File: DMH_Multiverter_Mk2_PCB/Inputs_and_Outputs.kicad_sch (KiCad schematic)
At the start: 27 parts, among them J1 TS_Jack_6.35mm_Sw, J10 TS_Jack_6.35mm_Sw, J11 TS_Jack_6.35mm_Sw, J12 TS_Jack_6.35mm_Sw, J13 TS_Jack_6.35mm_Sw, J14 TS_Jack_6.35mm_Sw, J15 TS_Jack_6.35mm_Sw, J16 TS_Jack_6.35mm_Sw, J17 TS_Jack_6.35mm_Sw, J18 TS_Jack_6.35mm_Sw, J19 TS_Jack_6.35mm_Sw, J2 TS_Jack_6.35mm_Sw, J20 TS_Jack_6.35mm_Sw, J200 BackBone_Connector_6pin, J21 TS_Jack_6.35mm_Sw, J22 TS_Jack_6.35mm_Sw, J3 TS_Jack_6.35mm_Sw, J4 TS_Jack_6.35mm_Sw, J5 TS_Jack_6.35mm_Sw, J50 Conn_01x06, J6 TS_Jack_6.35mm_Sw, J60 Conn_01x06, J7 TS_Jack_6.35mm_Sw, J8 TS_Jack_6.35mm_Sw, J9 TS_Jack_6.35mm_Sw

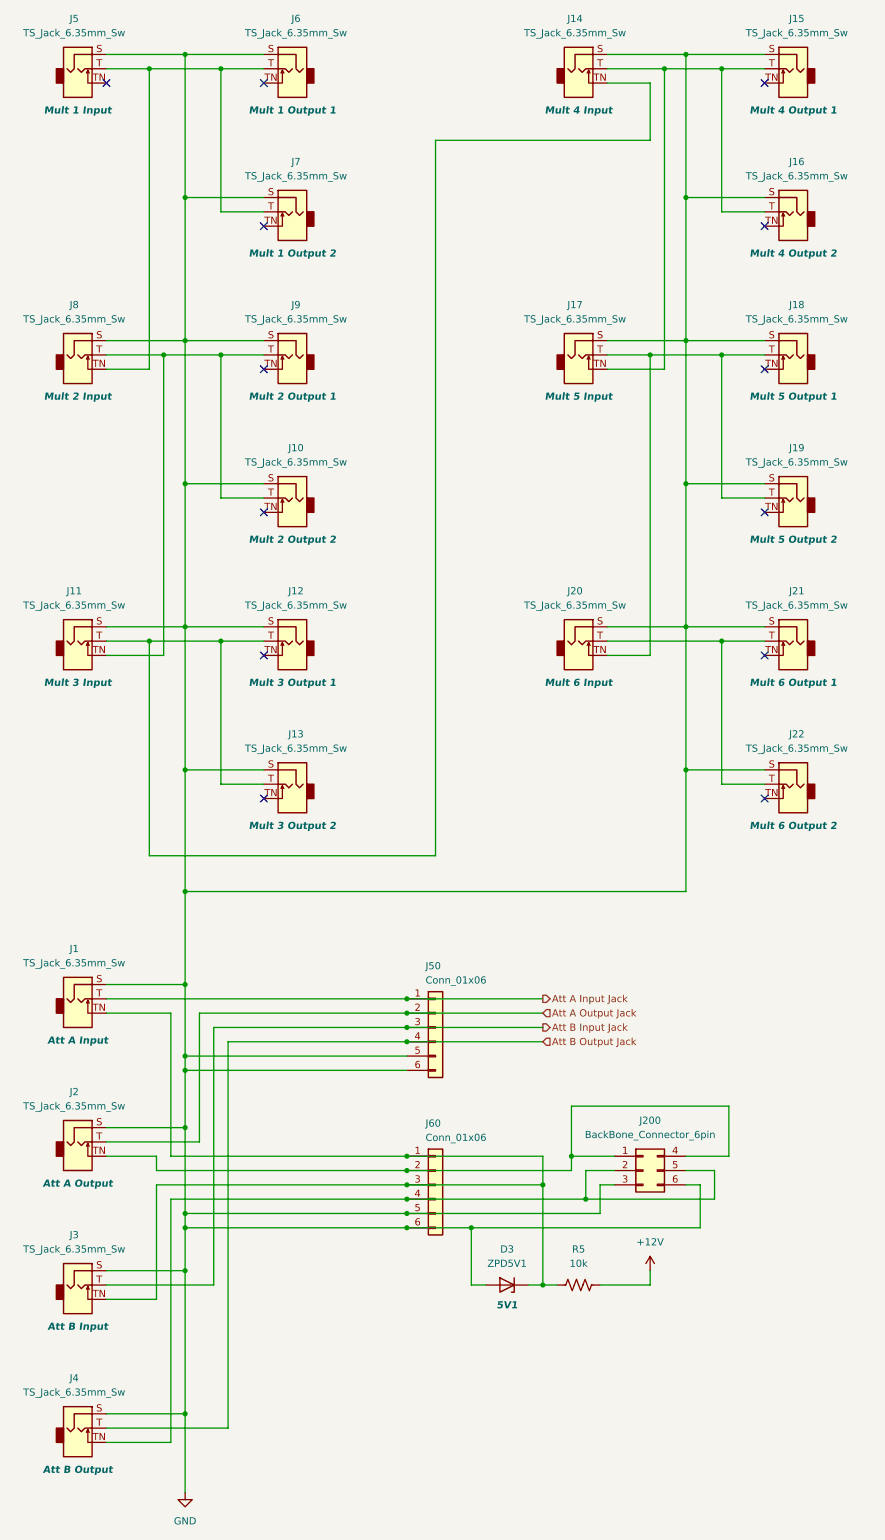
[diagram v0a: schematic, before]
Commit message: Added 3rd attenuverter to Panel and Schematic
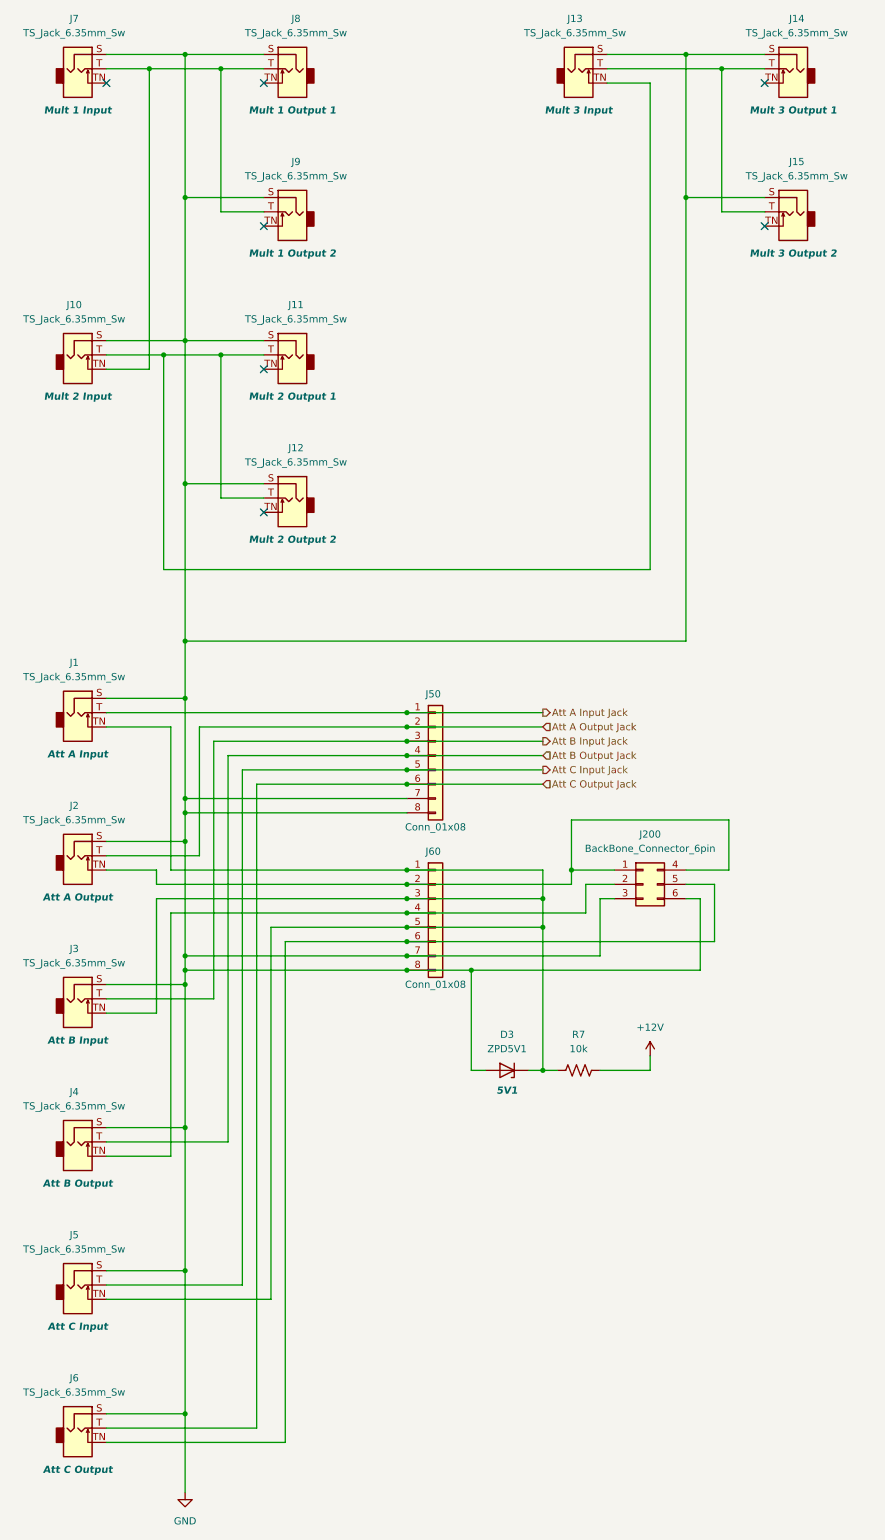
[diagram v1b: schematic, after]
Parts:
- removed J11, J12, J13, J17, J18, J19, J20, J21, J22: TS_Jack_6.35mm_Sw, SynthStuff:CUI_MJ-63052A, symbol SynthStuff:TS_Jack_6.35mm_Sw
- added J5, J6: TS_Jack_6.35mm_Sw, SynthStuff:CUI_MJ-63052A, symbol SynthStuff:TS_Jack_6.35mm_Sw
- J13: renamed from J14; Function Mult 4 Input -> Mult 3 Input
- J14: renamed from J15; Function Mult 4 Output 1 -> Mult 3 Output 1
- J15: renamed from J16; Function Mult 4 Output 2 -> Mult 3 Output 2
- J50, J60: value Conn_01x06 -> Conn_01x08; symbol Connector_Generic:Conn_01x06 -> Connector_Generic:Conn_01x08
- renumbered J8 to J10, J9 to J11, J10 to J12, J5 to J7, J6 to J8, J7 to J9, R5 to R7
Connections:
- net GND: now also J50.7 (Pin_7), J50.8 (Pin_8), J60.7 (Pin_7), J60.8 (Pin_8), J5.S, J6.S; no longer J50.5 (Pin_5), J50.6 (Pin_6), J60.5 (Pin_5), J60.6 (Pin_6)
- net at D3.1 (K), J1.TN, J3.TN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: now also J60.5 (Pin_5), J5.TN
- net at J13.TN: now also J10.T, J11.T, J12.T
- net at J200.2 (Pin_2), J4.TN, J60.4 (Pin_4): no longer J200.5 (Pin_5)
- new net: J200.5 (Pin_5), J6.TN, J60.6 (Pin_6)
- new net Att C Input Jack: J5.T, J50.5 (Pin_5)
- new net Att C Output Jack: J50.6 (Pin_6), J6.T
- no-connect marks 13 -> 7
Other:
- moved on the sheet: D3, J1, J2, J200, J3, J4, R7

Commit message: Main PCB components placed
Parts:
- J50, J60: footprint Connector_PinSocket_2.54mm:PinSocket_1x06_P2.54mm_Vertical -> Connector_PinSocket_2.54mm:PinSocket_1x08_P2.54mm_Vertical
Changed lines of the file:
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@@
 			)
 		)
-		(property "Footprint" "Connector_PinSocket_2.54mm:PinSocket_1x06_P2.54mm_Vertical"
+		(property "Footprint" "Connector_PinSocket_2.54mm:PinSocket_1x08_P2.54mm_Vertical"
 			(at 88.9 147.32 0)
 			(effects
@@
 			)
 		)
-		(property "Footprint" "Connector_PinSocket_2.54mm:PinSocket_1x06_P2.54mm_Vertical"
+		(property "Footprint" "Connector_PinSocket_2.54mm:PinSocket_1x08_P2.54mm_Vertical"
 			(at 88.9 175.26 0)
 			(effects

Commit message: Routed Connectors PCB
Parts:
- J50, J60: footprint Connector_PinSocket_2.54mm:PinSocket_1x08_P2.54mm_Vertical -> Connector_PinHeader_2.54mm:PinHeader_1x08_P2.54mm_Vertical
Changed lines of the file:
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@@
 			)
 		)
-		(property "Footprint" "Connector_PinSocket_2.54mm:PinSocket_1x08_P2.54mm_Vertical"
+		(property "Footprint" "Connector_PinHeader_2.54mm:PinHeader_1x08_P2.54mm_Vertical"
 			(at 88.9 147.32 0)
 			(effects
@@
 			)
 		)
-		(property "Footprint" "Connector_PinSocket_2.54mm:PinSocket_1x08_P2.54mm_Vertical"
+		(property "Footprint" "Connector_PinHeader_2.54mm:PinHeader_1x08_P2.54mm_Vertical"
 			(at 88.9 175.26 0)
 			(effects

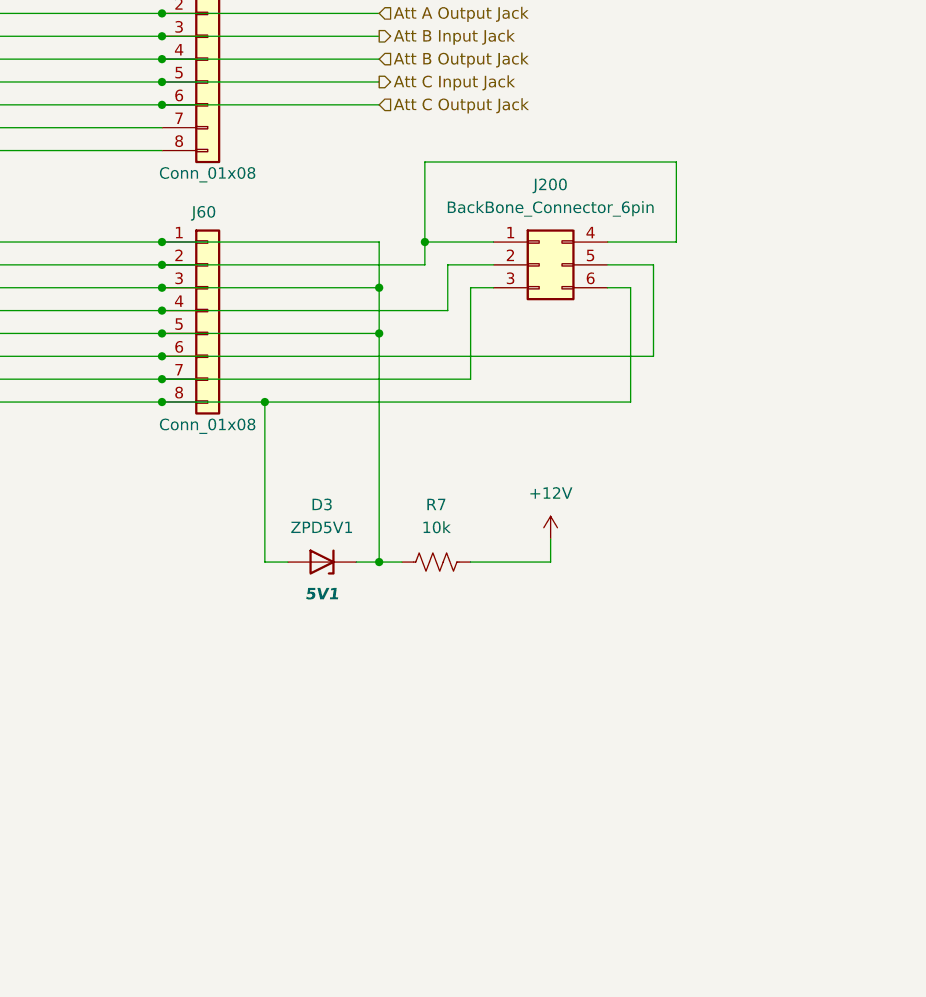
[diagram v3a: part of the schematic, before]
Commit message: Independent zeners for normalled 5V DC offset
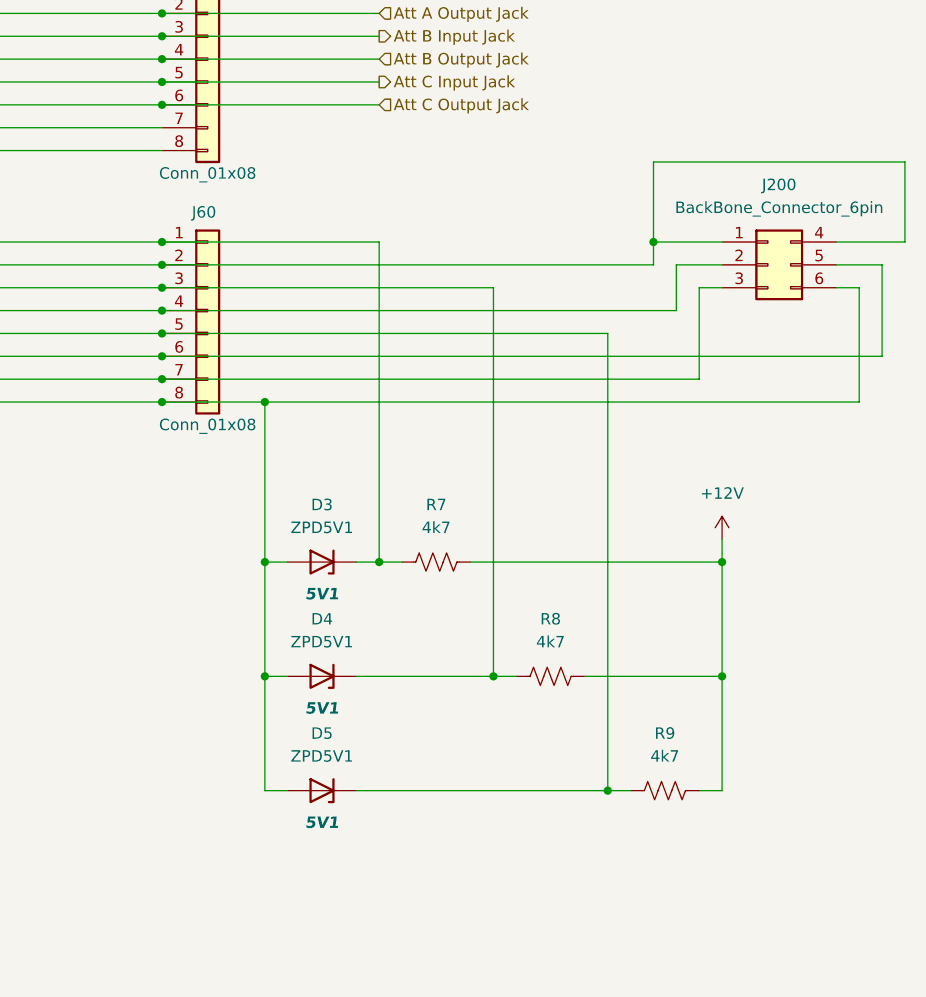
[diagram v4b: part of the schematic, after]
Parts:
- added D4, D5: ZPD5V1, Diode_THT:D_DO-35_SOD27_P7.62mm_Horizontal, symbol Diode:ZPDxx
- added R8, R9: 4k7, Resistor_THT:R_Axial_DIN0207_L6.3mm_D2.5mm_P7.62mm_Horizontal, symbol Device:R_US
- R7: value 10k -> 4k7
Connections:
- net +12V: now also R8.2, R9.2
- net GND: now also D4.2 (A), D5.2 (A)
- net at D3.1 (K), J1.TN, J60.1 (Pin_1)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: no longer J3.TN, J5.TN, J60.3 (Pin_3), J60.5 (Pin_5)
- new net: D4.1 (K), J3.TN, J60.3 (Pin_3), R8.1
- new net: D5.1 (K), J5.TN, J60.5 (Pin_5), R9.1
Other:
- moved on the sheet: J200
